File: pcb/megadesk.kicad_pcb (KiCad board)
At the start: 2 copper layers, 41.7 x 32.2 mm, 24 parts, among them J1 Interface, J2 FFC, J3 AVR-ISP-6, U1 7812, U2 HT7550-1, U3 ATtiny841-SS, U4 MCP2003B

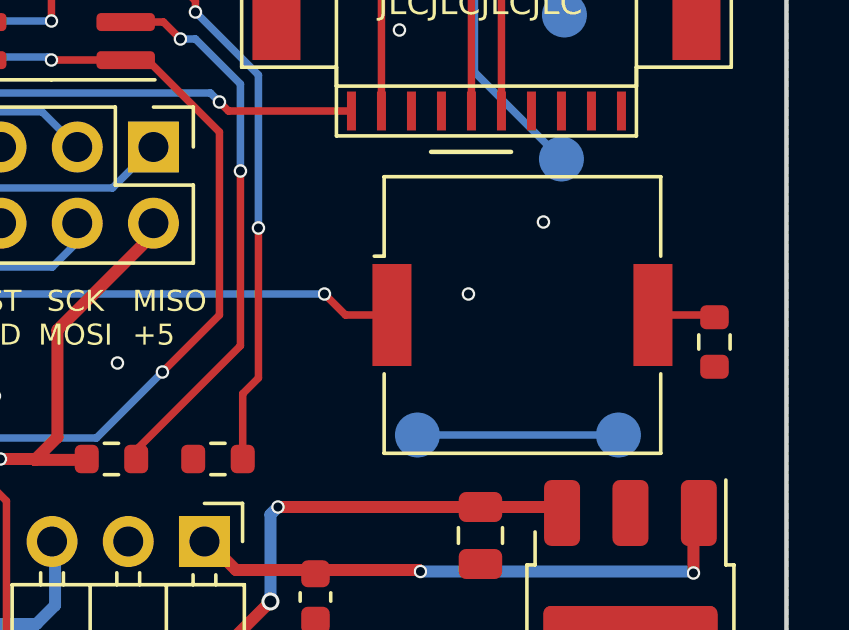
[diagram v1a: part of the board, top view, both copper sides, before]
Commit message: buzzer polarity silkscreen
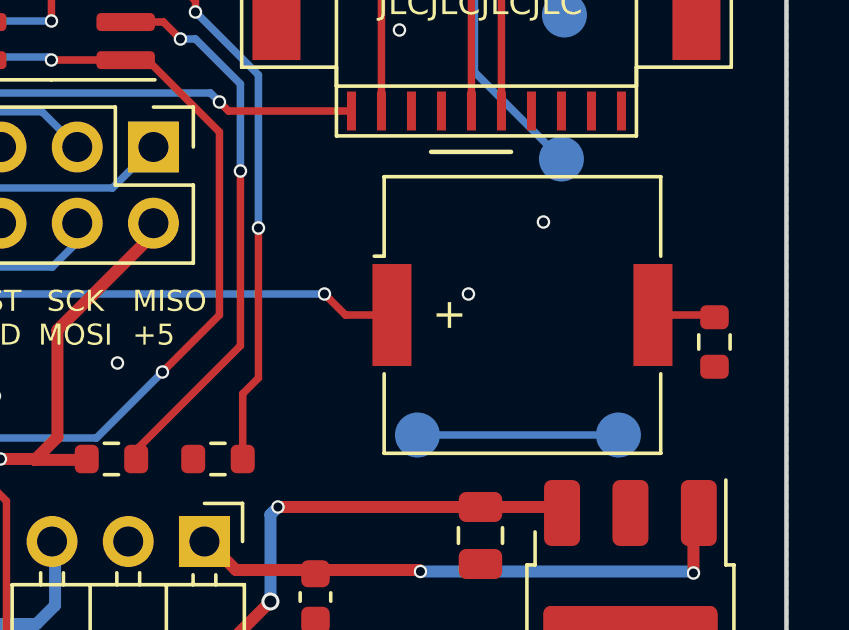
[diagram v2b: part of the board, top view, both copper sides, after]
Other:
- board text added: "+"
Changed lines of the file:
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@@
     (effects (font (size 0.8 0.8) (thickness 0.125)))
+  )
+  (gr_text "+" (at 129.7 118.8 270) (layer "F.SilkS")
+    (effects (font (size 1 1) (thickness 0.15)))
   )
   (gr_text "RST\nGND" (at 115.4 118.9) (layer "F.SilkS")

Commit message: 5pin ver
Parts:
- removed J1: Interface, Connector_PinHeader_2.54mm:PinHeader_1x03_P2.54mm_Horizontal
- added J4: Interface, Connector_PinHeader_2.54mm:PinHeader_1x05_P2.54mm_Horizontal, F.Cu at (126.6, 126.5)
- moved C1 14.8 mm to (138.4, 121.5), turned to 90 degrees
- moved R1 4.15 mm to (138.4, 115.5), turned to 90 degrees
- moved R3 0.52 mm to (108.5, 125.1)
- moved C3 0.25 mm to (130.4, 126.2)
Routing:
- net SCK: track 9.91 -> 28.6 mm, vias 1 -> 3
- net MISO: track 12.4 -> 28.8 mm, vias 1 -> 3
- net LINBUS: track 29.6 -> 34.2 mm
- net GND: track 3.18 -> 0.00 mm, vias 23 -> 24
- net Net-(BZ1-+): track 1.98 -> 3.97 mm
- net Net-(U3-PA2): track 36.7 -> 37.6 mm
- net +24V: track 18.5 -> 17.7 mm, vias 2 -> 0
- net +5V: track 54.9 -> 54.1 mm
- net +12V: track 36.3 -> 35.9 mm, vias 10 -> 8
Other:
- board text added: "megadesk v11"
- board text removed: "megadesk v10"

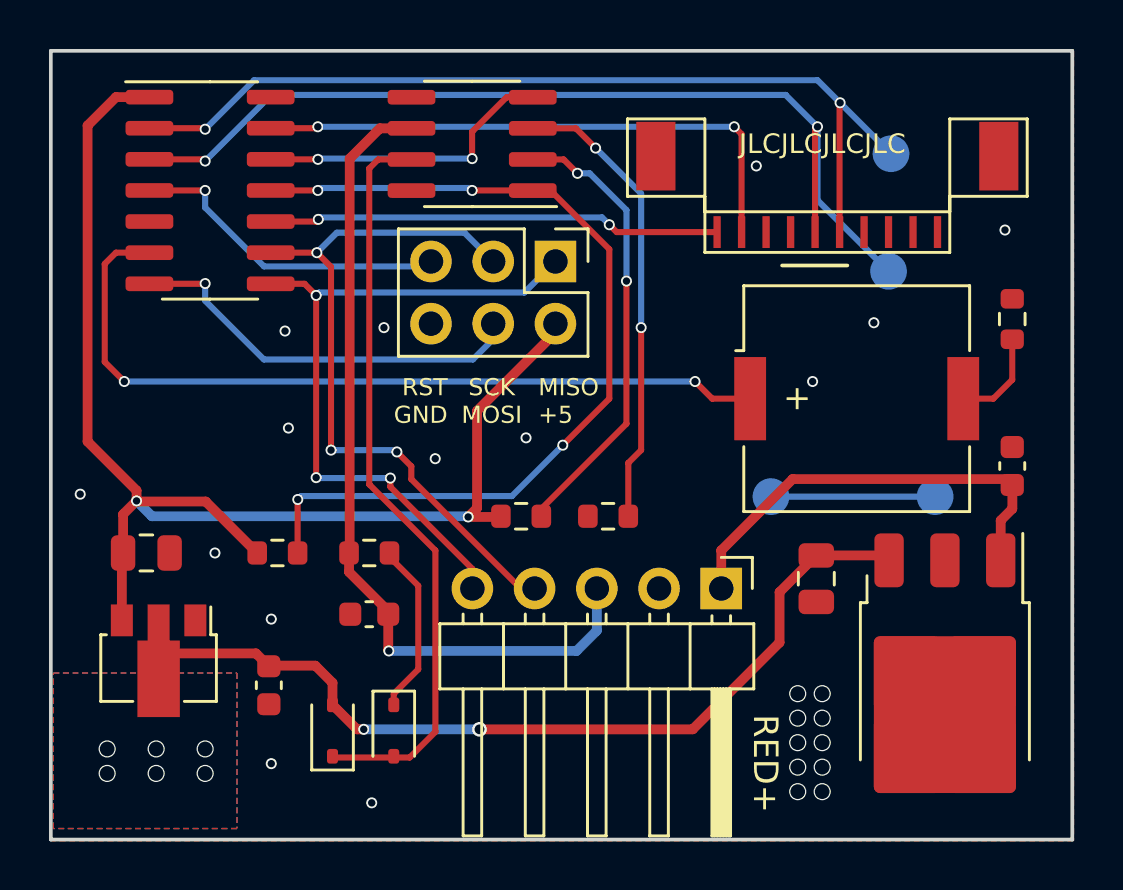
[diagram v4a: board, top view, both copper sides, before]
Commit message: update v12 5pin
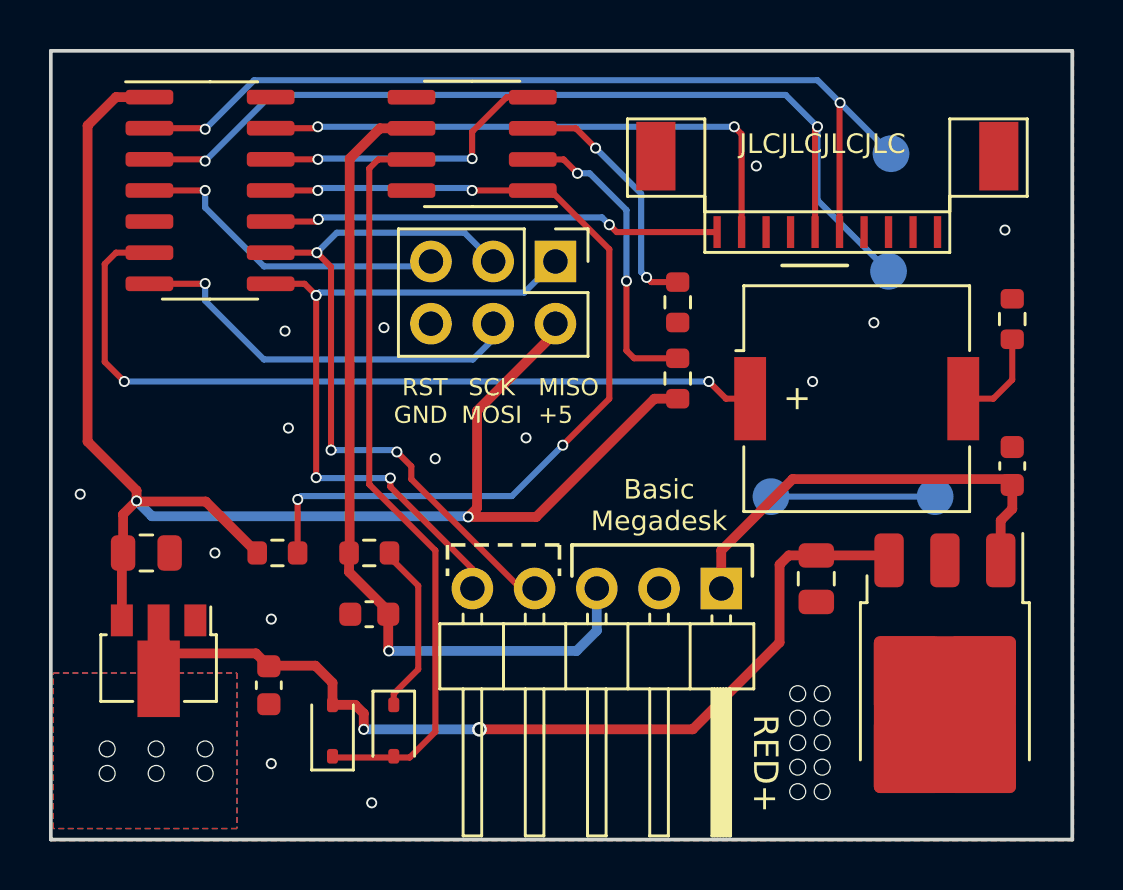
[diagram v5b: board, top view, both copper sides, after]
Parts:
- moved R5 9.18 mm to (124.8, 114.9), turned to -90 degrees
- moved R4 8.51 mm to (124.8, 118.0), turned to -90 degrees
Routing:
- net +5V: track 54.1 -> 63.4 mm
- net Net-(U4-WAKE): track 18.9 -> 10.4 mm
- net Net-(U4-CS): track 18.3 -> 12.6 mm
- net +12V: track 35.9 -> 36.9 mm
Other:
- board text added: "Basic Megadesk"
